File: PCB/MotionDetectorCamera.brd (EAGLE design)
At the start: 211.5 x 44.5 mm, 186 parts, among them J1 JUMPER-SOLDER, J12 JUMPER-AMPHENOL-10129380-9020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, J13 JUMPER-AMPHENOL-10129380-9020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, J14 JUMPER-AMPHENOL-10129380-9020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, J15 JUMPER-AMPHENOL-10129380-9020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, J2 JUMPER-SOLDER, J4 JUMPER-AMPHENOL-10129380-9020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, J5 JUMPER-SOLDER, J6 S-MOUNT-LENS-HOLDER, J7 MICROSD-SOCKET, J8 MINI-USB-JACK, Q1 PMOS-NEXPERIA-SOT1220, Q10 PMOS-NEXPERIA-SOT1220, Q2 PMOS-NEXPERIA-SOT1220, Q3 PMOS-NEXPERIA-SOT1220, U1 NEXPERIA-74LVC1G98-BUFFER, U10 TI-TPS22919DCK, U11 TI-TPS2116, U12 TI-MSP430FR2422IRHL, U14 PANASONIC-EKMB110711X, U15 LATTICE-ICE40HX4K-BG121, U16 MICROCHIP-MCP7383X, U17 ON-AR0330CS1C12SPKA0, U18 ALLIANCE-AS4C8M16MSA-6BIN, U19 STM-STM32F730, U2 DIODESINC-AP7350, U20 DIODESINC-DT1446-04V-7, U21 NXP-NTB0102, U22 NXP-NTB0102, U23 TI-TPS6280XYKAR, U24 NEXPERIA-74LVC1G98-OR-INV-INP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, U28 NEXPERIA-74LVC1G98-NOR, U3 TI-TPS6280XYKAR, U30 TI-TPS22919DCK, U4 TI-TPS6280XYKAR, U5 WINBOND-W25Q40EW, U6 TI-TPS22919DCK, U7 TI-TPS22919DCK, U8 TI-TPS22919DCK, U9 TI-TPS22919DCK, X1 EPSON-FC-135, X2 SITIME-SIT8021, X3 SITIME-SIT8021

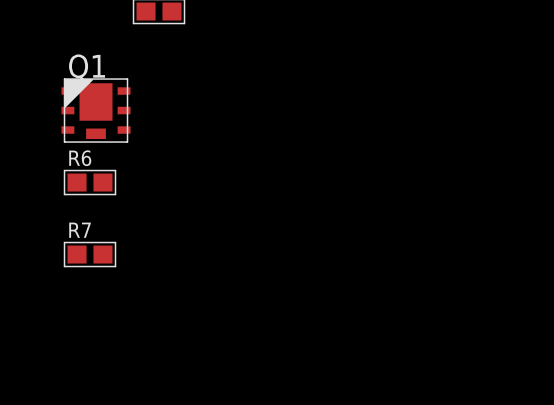
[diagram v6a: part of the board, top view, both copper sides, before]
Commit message: Add ESD protection to VDD_BAT
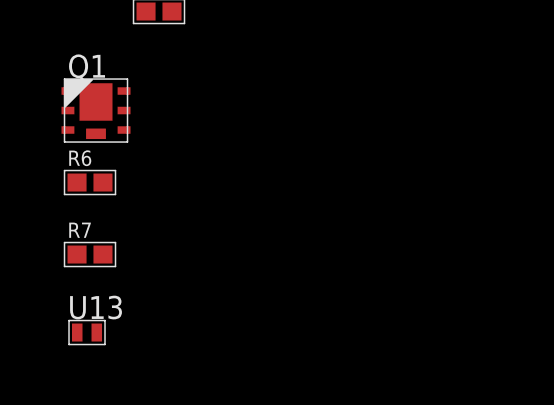
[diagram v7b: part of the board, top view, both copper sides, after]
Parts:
- added U13: EATON-STN101, EagleLibrary:EATON-STN101
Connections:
- net GND: now also U13.2
- net N$35: now also U13.1
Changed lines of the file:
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@@
 <attribute name="PN" value="RMCF0402JT100K" x="-14.9" y="-171.1" size="1.778" layer="27" display="off"/>
 </element>
+<element name="U13" library="EagleLibrary" package="EATON-STN101" value="EATON-STN101" x="-15" y="-173.7" smashed="yes">
+<attribute name="MFG" value="Eaton" x="-15" y="-173.7" size="1.778" layer="27" display="off"/>
+<attribute name="NAME" x="-15.645559375" y="-173.24761875" size="0.762" layer="25" font="vector"/>
+</element>
 </elements>
 <signals>
@@
 <contactref element="C88" pad="2"/>
 <contactref element="R35" pad="2"/>
+<contactref element="U13" pad="2"/>
+<wire x1="-12.1675" y1="-163" x2="-14.675" y2="-173.7" width="0" layer="19" extent="1-1"/>
 <wire x1="-13.1246" y1="-158.2" x2="-12.1675" y2="-163" width="0" layer="19" extent="1-1"/>
 <wire x1="-14.2675" y1="-155" x2="-13.1246" y2="-158.2" width="0" layer="19" extent="1-1"/>
@@
 <contactref element="R4" pad="1"/>
 <contactref element="J4" pad="2"/>
+<contactref element="U13" pad="1"/>
+<wire x1="-12.23" y1="-47.315" x2="-15.325" y2="-173.7" width="0" layer="19" extent="1-1"/>
 <wire x1="-15.1325" y1="-39.7" x2="-12.23" y2="-47.315" width="0" layer="19" extent="1-1"/>
 <wire x1="-15.435" y1="-34.9" x2="-15.1325" y2="-39.7" width="0" layer="19" extent="1-1"/>

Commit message: Connect to STM32: BAT_CHRG_STAT, BAT_CHRG_LVL, BAT_CHRG_LVL_EN_
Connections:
- net BAT_CHRG_LVL: now also U19.P5
- net BAT_CHRG_LVL_EN_: now also U19.N5
- net BAT_CHRG_STAT: now also U19.M5
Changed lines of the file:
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@@
 <layers>
 <layer number="1" name="Top" color="4" fill="1" visible="yes" active="yes"/>
-<layer number="2" name="Ground" color="16" fill="1" visible="no" active="yes"/>
+<layer number="2" name="Ground" color="16" fill="1" visible="yes" active="yes"/>
 <layer number="3" name="Route3" color="17" fill="1" visible="no" active="no"/>
 <layer number="4" name="Route4" color="18" fill="1" visible="no" active="no"/>
@@
 <layer number="13" name="Route13" color="21" fill="1" visible="no" active="no"/>
 <layer number="14" name="Route14" color="22" fill="1" visible="no" active="no"/>
-<layer number="15" name="Power" color="42" fill="1" visible="no" active="yes"/>
-<layer number="16" name="Bottom" color="1" fill="1" visible="no" active="yes"/>
+<layer number="15" name="Power" color="42" fill="1" visible="yes" active="yes"/>
+<layer number="16" name="Bottom" color="1" fill="1" visible="yes" active="yes"/>
 <layer number="17" name="Pads" color="2" fill="1" visible="yes" active="yes"/>
 <layer number="18" name="Vias" color="2" fill="1" visible="yes" active="yes"/>
@@
 <layer number="20" name="Dimension" color="24" fill="1" visible="yes" active="yes"/>
 <layer number="21" name="tPlace" color="7" fill="1" visible="yes" active="yes"/>
-<layer number="22" name="bPlace" color="7" fill="1" visible="no" active="yes"/>
+<layer number="22" name="bPlace" color="7" fill="1" visible="yes" active="yes"/>
 <layer number="23" name="tOrigins" color="15" fill="1" visible="yes" active="yes"/>
-<layer number="24" name="bOrigins" color="15" fill="1" visible="no" active="yes"/>
+<layer number="24" name="bOrigins" color="15" fill="1" visible="yes" active="yes"/>
 <layer number="25" name="tNames" color="7" fill="1" visible="yes" active="yes"/>
-<layer number="26" name="bNames" color="7" fill="1" visible="no" active="yes"/>
+<layer number="26" name="bNames" color="7" fill="1" visible="yes" active="yes"/>
 <layer number="27" name="tValues" color="7" fill="1" visible="yes" active="yes"/>
-<layer number="28" name="bValues" color="7" fill="1" visible="no" active="yes"/>
+<layer number="28" name="bValues" color="7" fill="1" visible="yes" active="yes"/>
 <layer number="29" name="tStop" color="7" fill="3" visible="yes" active="yes"/>
-<layer number="30" name="bStop" color="7" fill="6" visible="no" active="yes"/>
-<layer number="31" name="tCream" color="7" fill="4" visible="yes" active="yes"/>
+<layer number="30" name="bStop" color="7" fill="6" visible="yes" active="yes"/>
+<layer number="31" name="tCream" color="7" fill="4" visible="no" active="yes"/>
 <layer number="32" name="bCream" color="7" fill="5" visible="no" active="yes"/>
-<layer number="33" name="tFinish" color="6" fill="3" visible="yes" active="yes"/>
+<layer number="33" name="tFinish" color="6" fill="3" visible="no" active="yes"/>
 <layer number="34" name="bFinish" color="6" fill="6" visible="no" active="yes"/>
-<layer number="35" name="tGlue" color="7" fill="4" visible="yes" active="yes"/>
+<layer number="35" name="tGlue" color="7" fill="4" visible="no" active="yes"/>
 <layer number="36" name="bGlue" color="7" fill="5" visible="no" active="yes"/>
-<layer number="37" name="tTest" color="7" fill="1" visible="yes" active="yes"/>
+<layer number="37" name="tTest" color="7" fill="1" visible="no" active="yes"/>
 <layer number="38" name="bTest" color="7" fill="1" visible="no" active="yes"/>
 <layer number="39" name="tKeepout" color="4" fill="11" visible="no" active="yes"/>
 <layer number="40" name="bKeepout" color="1" fill="11" visible="no" active="yes"/>
 <layer number="41" name="tRestrict" color="4" fill="10" visible="yes" active="yes"/>
-<layer number="42" name="bRestrict" color="1" fill="10" visible="no" active="yes"/>
-<layer number="43" name="vRestrict" color="2" fill="10" visible="no" active="yes"/>
+<layer number="42" name="bRestrict" color="1" fill="10" visible="yes" active="yes"/>
+<layer number="43" name="vRestrict" color="2" fill="10" visible="yes" active="yes"/>
 <layer number="44" name="Drills" color="7" fill="1" visible="no" active="yes"/>
 <layer number="45" name="Holes" color="7" fill="1" visible="no" active="yes"/>
 <layer number="46" name="Milling" color="3" fill="1" visible="no" active="yes"/>
 <layer number="47" name="Measures" color="7" fill="1" visible="no" active="yes"/>
-<layer number="48" name="Document" color="7" fill="1" visible="no" active="yes"/>
+<layer number="48" name="Document" color="7" fill="1" visible="yes" active="yes"/>
 <layer number="49" name="Reference" color="7" fill="1" visible="no" active="yes"/>
 <layer number="50" name="dxf" color="7" fill="1" visible="no" active="no"/>
@@
 <signal name="BAT_CHRG_STAT">
 <contactref element="U16" pad="1"/>
+<contactref element="U19" pad="M5"/>
+<wire x1="23.4754" y1="14.0624" x2="100.1356" y2="6.15" width="0" layer="19" extent="1-1"/>
 </signal>
 <signal name="BAT_CHRG_LVL">
 <contactref element="R35" pad="1"/>
 <contactref element="R6" pad="2"/>
+<contactref element="U19" pad="P5"/>
 <wire x1="-13.0325" y1="-163" x2="-14.4675" y2="-168.7" width="0" layer="19" extent="1-1"/>
+<wire x1="23.4754" y1="12.7624" x2="-13.0325" y2="-163" width="0" layer="19" extent="1-1"/>
 </signal>
 <signal name="N$46">
@@
 <contactref element="Q1" pad="3"/>
 <contactref element="R7" pad="2"/>
+<contactref element="U19" pad="N5"/>
 <wire x1="-15.635" y1="-166.95" x2="-14.4675" y2="-171.1" width="0" layer="19" extent="1-1"/>
+<wire x1="23.4754" y1="13.4124" x2="-15.635" y2="-166.95" width="0" layer="19" extent="1-1"/>
 </signal>
 </signals>
